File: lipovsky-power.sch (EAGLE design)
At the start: 100 parts, among them Q11 NMOS40V_10A, Q12 NMOS40V_10A, Q14 NMOS40V_10A, Q15 NMOS40V_10A, Q16 NMOS40V_10A, Q18 NMOS40V_10A, Q2 2NMOS30V_0.1A, Q21 PMOS30V_11A, Q22 PMOS30V_11A, Q23 NMOS40V_10A, Q24 NMOS40V_10A, Q25 PMOS30V_11A, Q26 PMOS30V_11A, Q27 NMOS40V_10A, Q28 NMOS40V_10A, Q3 2PMOS50V_0.17A, Q31 PMOS30V_11A, Q32 PMOS30V_11A, Q33 PMOS30V_11A, Q34 PMOS30V_11A, Q35 PMOS30V_11A, Q36 PMOS30V_11A, Q37 PMOS30V_11A, Q38 PMOS30V_11A, Q4 2PMOS50V_0.17A, Q41 PMOS30V_11A, Q42 PMOS30V_11A, Q43 PMOS30V_11A, Q44 PMOS30V_11A, Q45 PMOS30V_11A, Q46 PMOS30V_11A, Q47 PMOS30V_11A, Q48 PMOS30V_11A, Q5 2NMOS30V_0.1A, Q51 PMOS30V_11A, Q52 PMOS30V_11A, Q53 PMOS30V_11A, Q54 PMOS30V_11A, Q55 PMOS30V_11A, Q56 PMOS30V_11A, Q57 PMOS30V_11A, Q58 PMOS30V_11A, Q62 PMOS30V_11A, Q64 PMOS30V_11A, Q66 PMOS30V_11A, Q68 PMOS30V_11A, T1 TFORM_4_4311_4A4, U1 DG508BEN-T1-GE4, U2 DG508BEN-T1-GE4, U3 74HC595, U4 LTC3805-5IDD, U5 TC1240A, U6 AR30N60PPA-13

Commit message: .
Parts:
- removed C6: CAP4.7U_10V, dubec:CAP4.7U_10V
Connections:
- net MVOE renamed GS-2
- net N$7 renamed SENSE
- new net S-SENSE: C2.1, C4.1, D4.A, R5.1, R6.1, U4.GND, U4.OC, U4.SYNC
- net S-: no longer C2.1, C4.1, C6.1, D4.A, R5.1, R6.1, U4.GND, U4.OC, U4.SYNC
- net VCC_REG: no longer C6.2
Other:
- moved on the sheet: C2
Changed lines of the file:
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@@
 <part name="R18" library="dubec" deviceset="RES" device="5.1K_16"/>
 <part name="Q5" library="dubec" deviceset="2NMOS" device="30V_0.1A"/>
-<part name="C6" library="dubec" deviceset="CAP" device="4.7U_10V" value="CAP4.7U_10V"/>
 </parts>
 <sheets>
@@
 <instance part="R7" gate="G$1" x="55.88" y="-66.04"/>
 <instance part="C4" gate="G$1" x="50.8" y="-73.66" rot="R90"/>
-<instance part="C2" gate="G$1" x="53.34" y="-45.72" rot="R90"/>
+<instance part="C2" gate="G$1" x="50.8" y="-45.72" rot="R90"/>
 <instance part="C1" gate="G$1" x="15.24" y="-38.1" rot="R90"/>
 <instance part="C5" gate="G$1" x="73.66" y="-27.94" rot="R90"/>
@@
 <instance part="D2" gate="G$1" x="35.56" y="73.66" rot="R90"/>
 <instance part="D2" gate="G$2" x="27.94" y="53.34" rot="R90"/>
-<instance part="C6" gate="G$1" x="45.72" y="-45.72" rot="R90"/>
 </instances>
 <busses>
@@
 </segment>
 <segment>
-<pinref part="U5" gate="G$1" pin="GND"/>
-<wire x1="30.48" y1="-48.26" x2="30.48" y2="-50.8" width="0.1524" layer="91"/>
-<pinref part="U5" gate="G$1" pin="SHDN"/>
-<pinref part="C2" gate="G$1" pin="1"/>
-<wire x1="76.2" y1="-71.12" x2="76.2" y2="-78.74" width="0.1524" layer="91"/>
-<label x="76.2" y="-81.28" size="1.778" layer="95" rot="R270" xref="yes"/>
-<wire x1="76.2" y1="-78.74" x2="76.2" y2="-81.28" width="0.1524" layer="91"/>
-<junction x="76.2" y="-78.74"/>
-<pinref part="R6" gate="G$1" pin="1"/>
-<wire x1="53.34" y1="-60.96" x2="43.18" y2="-60.96" width="0.1524" layer="91"/>
-<wire x1="43.18" y1="-78.74" x2="50.8" y2="-78.74" width="0.1524" layer="91"/>
-<wire x1="50.8" y1="-78.74" x2="76.2" y2="-78.74" width="0.1524" layer="91"/>
-<wire x1="43.18" y1="-60.96" x2="43.18" y2="-78.74" width="0.1524" layer="91"/>
-<pinref part="C4" gate="G$1" pin="1"/>
-<wire x1="50.8" y1="-76.2" x2="50.8" y2="-78.74" width="0.1524" layer="91"/>
-<junction x="50.8" y="-78.74"/>
-<wire x1="43.18" y1="-50.8" x2="43.18" y2="-60.96" width="0.1524" layer="91"/>
-<junction x="43.18" y="-60.96"/>
-<junction x="43.18" y="-50.8"/>
-<wire x1="30.48" y1="-50.8" x2="40.64" y2="-50.8" width="0.1524" layer="91"/>
-<pinref part="C5" gate="G$1" pin="1"/>
-<wire x1="40.64" y1="-50.8" x2="43.18" y2="-50.8" width="0.1524" layer="91"/>
-<wire x1="73.66" y1="-30.48" x2="73.66" y2="-33.02" width="0.1524" layer="91"/>
-<wire x1="73.66" y1="-33.02" x2="40.64" y2="-33.02" width="0.1524" layer="91"/>
-<pinref part="R5" gate="G$1" pin="1"/>
-<wire x1="104.14" y1="-71.12" x2="104.14" y2="-78.74" width="0.1524" layer="91"/>
-<wire x1="76.2" y1="-78.74" x2="93.98" y2="-78.74" width="0.1524" layer="91"/>
-<wire x1="93.98" y1="-78.74" x2="99.06" y2="-78.74" width="0.1524" layer="91"/>
-<pinref part="U4" gate="G$1" pin="GND"/>
-<pinref part="U4" gate="G$1" pin="SYNC"/>
-<wire x1="99.06" y1="-78.74" x2="104.14" y2="-78.74" width="0.1524" layer="91"/>
-<wire x1="60.96" y1="-50.8" x2="53.34" y2="-50.8" width="0.1524" layer="91"/>
-<pinref part="U4" gate="G$1" pin="OC"/>
-<wire x1="53.34" y1="-50.8" x2="45.72" y2="-50.8" width="0.1524" layer="91"/>
-<wire x1="45.72" y1="-50.8" x2="43.18" y2="-50.8" width="0.1524" layer="91"/>
-<wire x1="91.44" y1="-53.34" x2="93.98" y2="-53.34" width="0.1524" layer="91"/>
-<wire x1="93.98" y1="-53.34" x2="93.98" y2="-78.74" width="0.1524" layer="91"/>
-<junction x="93.98" y="-78.74"/>
-<junction x="104.14" y="-78.74"/>
-<wire x1="119.38" y1="-78.74" x2="104.14" y2="-78.74" width="0.1524" layer="91"/>
-<wire x1="99.06" y1="-71.12" x2="99.06" y2="-78.74" width="0.1524" layer="91"/>
-<junction x="99.06" y="-78.74"/>
-<pinref part="D4" gate="G$1" pin="A"/>
-<pinref part="Q5" gate="G$1" pin="S"/>
-<wire x1="119.38" y1="-60.96" x2="119.38" y2="-78.74" width="0.1524" layer="91"/>
-<pinref part="C6" gate="G$1" pin="1"/>
-<junction x="45.72" y="-50.8"/>
-<wire x1="40.64" y1="-33.02" x2="40.64" y2="-50.8" width="0.1524" layer="91"/>
-<junction x="40.64" y="-33.02"/>
-<junction x="40.64" y="-50.8"/>
-<wire x1="53.34" y1="-48.26" x2="53.34" y2="-50.8" width="0.1524" layer="91"/>
-<junction x="53.34" y="-50.8"/>
-<wire x1="45.72" y1="-48.26" x2="45.72" y2="-50.8" width="0.1524" layer="91"/>
-</segment>
-<segment>
 <pinref part="U1" gate="G$1" pin="GND"/>
 <wire x1="121.92" y1="76.2" x2="124.46" y2="76.2" width="0.1524" layer="91"/>
@@
 <pinref part="C8" gate="G$1" pin="1"/>
 <wire x1="241.3" y1="76.2" x2="259.08" y2="76.2" width="0.1524" layer="91"/>
+</segment>
+<segment>
+<pinref part="U5" gate="G$1" pin="GND"/>
+<wire x1="30.48" y1="-48.26" x2="30.48" y2="-50.8" width="0.1524" layer="91"/>
+<wire x1="30.48" y1="-50.8" x2="40.64" y2="-50.8" width="0.1524" layer="91"/>
+<pinref part="U5" gate="G$1" pin="SHDN"/>
+<pinref part="C5" gate="G$1" pin="1"/>
+<wire x1="73.66" y1="-30.48" x2="73.66" y2="-33.02" width="0.1524" layer="91"/>
+<wire x1="73.66" y1="-33.02" x2="40.64" y2="-33.02" width="0.1524" layer="91"/>
+<wire x1="40.64" y1="-33.02" x2="40.64" y2="-50.8" width="0.1524" layer="91"/>
+<junction x="40.64" y="-33.02"/>
+<label x="30.48" y="-53.34" size="1.778" layer="95" rot="R270" xref="yes"/>
+<wire x1="30.48" y1="-50.8" x2="30.48" y2="-53.34" width="0.1524" layer="91"/>
+<junction x="30.48" y="-50.8"/>
+</segment>
+<segment>
+<pinref part="Q5" gate="G$1" pin="S"/>
+<wire x1="119.38" y1="-60.96" x2="119.38" y2="-68.58" width="0.1524" layer="91"/>
+<label x="119.38" y="-68.58" size="1.778" layer="95" rot="R270" xref="yes"/>
 </segment>
 </net>
@@
 </segment>
 </net>
-<net name="MVOE" class="0">
+<net name="GS-2" class="0">
 <segment>
 <pinref part="Q23" gate="G$1" pin="G"/>
@@
 <pinref part="U5" gate="G$1" pin="VOUT"/>
 <wire x1="40.64" y1="-38.1" x2="43.18" y2="-38.1" width="0.1524" layer="91"/>
-<wire x1="43.18" y1="-38.1" x2="45.72" y2="-38.1" width="0.1524" layer="91"/>
-<wire x1="45.72" y1="-38.1" x2="53.34" y2="-38.1" width="0.1524" layer="91"/>
-<wire x1="53.34" y1="-38.1" x2="76.2" y2="-38.1" width="0.1524" layer="91"/>
+<wire x1="43.18" y1="-38.1" x2="50.8" y2="-38.1" width="0.1524" layer="91"/>
+<wire x1="50.8" y1="-38.1" x2="76.2" y2="-38.1" width="0.1524" layer="91"/>
 <wire x1="76.2" y1="-38.1" x2="76.2" y2="-40.64" width="0.1524" layer="91"/>
 <junction x="43.18" y="-38.1"/>
@@
 <wire x1="76.2" y1="-38.1" x2="119.38" y2="-38.1" width="0.1524" layer="91"/>
 <wire x1="119.38" y1="-38.1" x2="119.38" y2="-40.64" width="0.1524" layer="91"/>
-<junction x="45.72" y="-38.1"/>
-<pinref part="C6" gate="G$1" pin="2"/>
-<wire x1="45.72" y1="-40.64" x2="45.72" y2="-38.1" width="0.1524" layer="91"/>
-<wire x1="53.34" y1="-38.1" x2="53.34" y2="-40.64" width="0.1524" layer="91"/>
-<junction x="53.34" y="-38.1"/>
+<wire x1="50.8" y1="-38.1" x2="50.8" y2="-40.64" width="0.1524" layer="91"/>
+<junction x="50.8" y="-38.1"/>
 </segment>
 </net>
@@
 </segment>
 </net>
-<net name="N$7" class="0">
+<net name="SENSE" class="0">
 <segment>
 <pinref part="MVOE" gate="G$1" pin="S"/>
@@
 </segment>
 </net>
+<net name="S-SENSE" class="0">
+<segment>
+<pinref part="C2" gate="G$1" pin="1"/>
+<label x="43.18" y="-78.74" size="1.778" layer="95" rot="R180" xref="yes"/>
+<pinref part="R6" gate="G$1" pin="1"/>
+<wire x1="53.34" y1="-60.96" x2="45.72" y2="-60.96" width="0.1524" layer="91"/>
+<wire x1="45.72" y1="-78.74" x2="50.8" y2="-78.74" width="0.1524" layer="91"/>
+<wire x1="50.8" y1="-78.74" x2="76.2" y2="-78.74" width="0.1524" layer="91"/>
+<wire x1="45.72" y1="-60.96" x2="45.72" y2="-78.74" width="0.1524" layer="91"/>
+<pinref part="C4" gate="G$1" pin="1"/>
+<wire x1="50.8" y1="-76.2" x2="50.8" y2="-78.74" width="0.1524" layer="91"/>
+<junction x="50.8" y="-78.74"/>
+<wire x1="45.72" y1="-50.8" x2="45.72" y2="-60.96" width="0.1524" layer="91"/>
+<junction x="45.72" y="-60.96"/>
+<pinref part="U4" gate="G$1" pin="SYNC"/>
+<wire x1="60.96" y1="-50.8" x2="50.8" y2="-50.8" width="0.1524" layer="91"/>
+<wire x1="50.8" y1="-50.8" x2="45.72" y2="-50.8" width="0.1524" layer="91"/>
+<wire x1="50.8" y1="-48.26" x2="50.8" y2="-50.8" width="0.1524" layer="91"/>
+<junction x="50.8" y="-50.8"/>
+<pinref part="R5" gate="G$1" pin="1"/>
+<wire x1="104.14" y1="-71.12" x2="104.14" y2="-78.74" width="0.1524" layer="91"/>
+<wire x1="99.06" y1="-78.74" x2="104.14" y2="-78.74" width="0.1524" layer="91"/>
+<pinref part="D4" gate="G$1" pin="A"/>
+<wire x1="99.06" y1="-71.12" x2="99.06" y2="-78.74" width="0.1524" layer="91"/>
+<junction x="99.06" y="-78.74"/>
+<wire x1="93.98" y1="-78.74" x2="99.06" y2="-78.74" width="0.1524" layer="91"/>
+<pinref part="U4" gate="G$1" pin="OC"/>
+<wire x1="91.44" y1="-53.34" x2="93.98" y2="-53.34" width="0.1524" layer="91"/>
+<wire x1="93.98" y1="-53.34" x2="93.98" y2="-78.74" width="0.1524" layer="91"/>
+<wire x1="76.2" y1="-78.74" x2="93.98" y2="-78.74" width="0.1524" layer="91"/>
+<junction x="76.2" y="-78.74"/>
+<junction x="93.98" y="-78.74"/>
+<pinref part="U4" gate="G$1" pin="GND"/>
+<wire x1="76.2" y1="-78.74" x2="76.2" y2="-71.12" width="0.1524" layer="91"/>
+<wire x1="45.72" y1="-78.74" x2="43.18" y2="-78.74" width="0.1524" layer="91"/>
+<junction x="45.72" y="-78.74"/>
+</segment>
+</net>

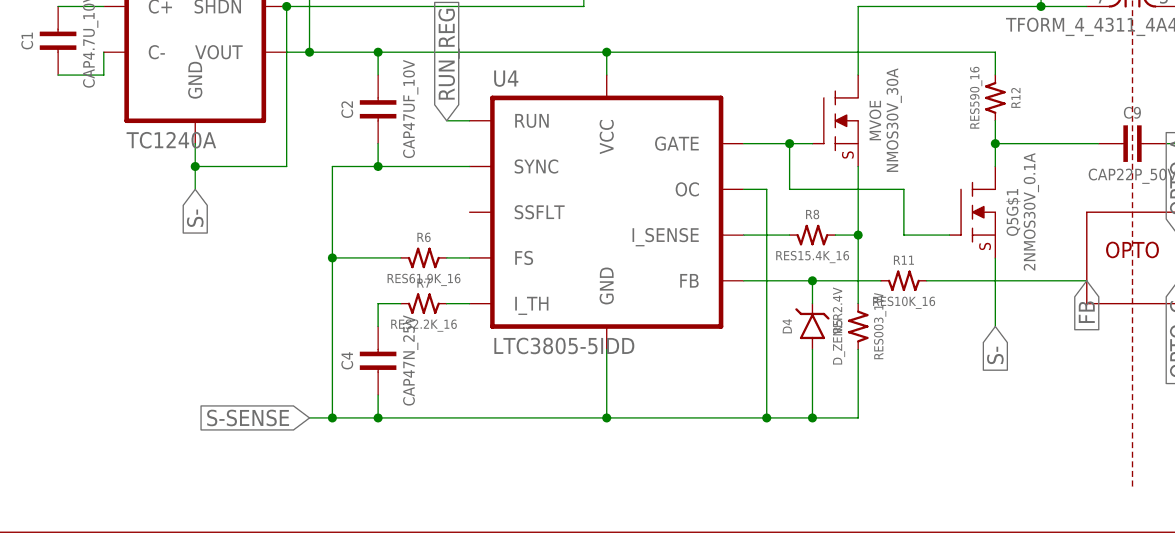
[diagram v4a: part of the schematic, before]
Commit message: Removed separate S-_SENSE
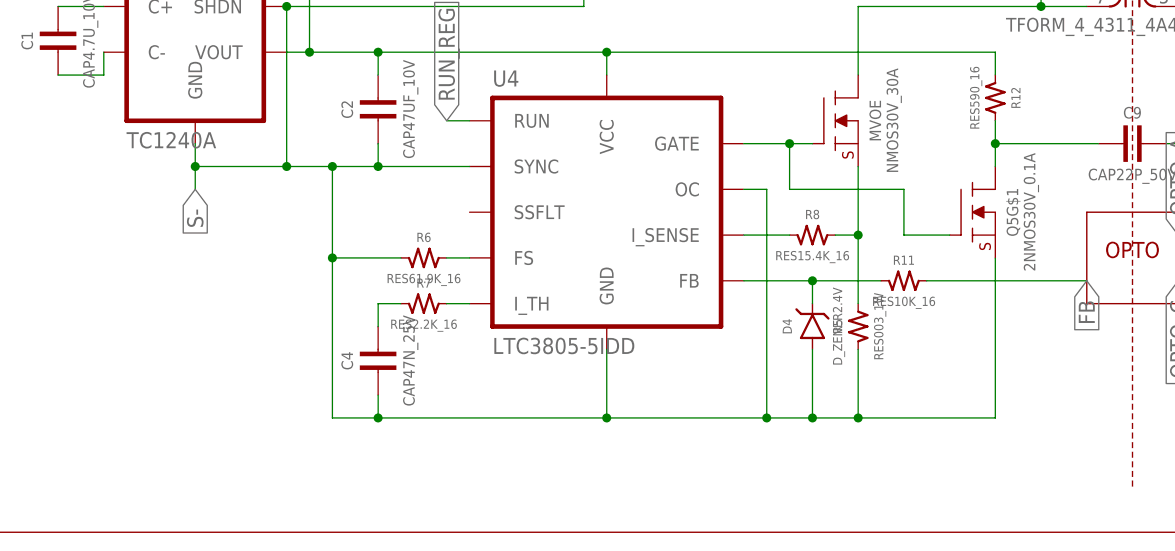
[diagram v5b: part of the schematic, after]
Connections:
- removed net S-SENSE: C2.1, C4.1, D4.A, R5.1, R6.1, U4.GND, U4.OC, U4.SYNC
- net S-: now also C2.1, C4.1, D4.A, R5.1, R6.1, U4.GND, U4.OC, U4.SYNC
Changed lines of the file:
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@@
 <wire x1="30.48" y1="-50.8" x2="30.48" y2="-53.34" width="0.1524" layer="91"/>
 <junction x="30.48" y="-50.8"/>
-</segment>
-<segment>
+<pinref part="C2" gate="G$1" pin="1"/>
+<pinref part="R6" gate="G$1" pin="1"/>
+<wire x1="53.34" y1="-60.96" x2="45.72" y2="-60.96" width="0.1524" layer="91"/>
+<wire x1="45.72" y1="-78.74" x2="50.8" y2="-78.74" width="0.1524" layer="91"/>
+<wire x1="50.8" y1="-78.74" x2="76.2" y2="-78.74" width="0.1524" layer="91"/>
+<wire x1="45.72" y1="-60.96" x2="45.72" y2="-78.74" width="0.1524" layer="91"/>
+<pinref part="C4" gate="G$1" pin="1"/>
+<wire x1="50.8" y1="-76.2" x2="50.8" y2="-78.74" width="0.1524" layer="91"/>
+<junction x="50.8" y="-78.74"/>
+<wire x1="45.72" y1="-50.8" x2="45.72" y2="-60.96" width="0.1524" layer="91"/>
+<junction x="45.72" y="-60.96"/>
+<pinref part="U4" gate="G$1" pin="SYNC"/>
+<wire x1="60.96" y1="-50.8" x2="50.8" y2="-50.8" width="0.1524" layer="91"/>
+<wire x1="50.8" y1="-50.8" x2="45.72" y2="-50.8" width="0.1524" layer="91"/>
+<wire x1="50.8" y1="-48.26" x2="50.8" y2="-50.8" width="0.1524" layer="91"/>
+<junction x="50.8" y="-50.8"/>
+<pinref part="R5" gate="G$1" pin="1"/>
+<wire x1="104.14" y1="-71.12" x2="104.14" y2="-78.74" width="0.1524" layer="91"/>
+<wire x1="99.06" y1="-78.74" x2="104.14" y2="-78.74" width="0.1524" layer="91"/>
+<pinref part="D4" gate="G$1" pin="A"/>
+<wire x1="99.06" y1="-71.12" x2="99.06" y2="-78.74" width="0.1524" layer="91"/>
+<junction x="99.06" y="-78.74"/>
+<wire x1="93.98" y1="-78.74" x2="99.06" y2="-78.74" width="0.1524" layer="91"/>
+<pinref part="U4" gate="G$1" pin="OC"/>
+<wire x1="91.44" y1="-53.34" x2="93.98" y2="-53.34" width="0.1524" layer="91"/>
+<wire x1="93.98" y1="-53.34" x2="93.98" y2="-78.74" width="0.1524" layer="91"/>
+<wire x1="76.2" y1="-78.74" x2="93.98" y2="-78.74" width="0.1524" layer="91"/>
+<junction x="76.2" y="-78.74"/>
+<junction x="93.98" y="-78.74"/>
+<pinref part="U4" gate="G$1" pin="GND"/>
+<wire x1="76.2" y1="-78.74" x2="76.2" y2="-71.12" width="0.1524" layer="91"/>
+<wire x1="40.64" y1="-50.8" x2="45.72" y2="-50.8" width="0.1524" layer="91"/>
+<junction x="40.64" y="-50.8"/>
+<junction x="45.72" y="-50.8"/>
+<wire x1="104.14" y1="-78.74" x2="119.38" y2="-78.74" width="0.1524" layer="91"/>
+<junction x="104.14" y="-78.74"/>
 <pinref part="Q5" gate="G$1" pin="S"/>
-<wire x1="119.38" y1="-60.96" x2="119.38" y2="-68.58" width="0.1524" layer="91"/>
-<label x="119.38" y="-68.58" size="1.778" layer="95" rot="R270" xref="yes"/>
+<wire x1="119.38" y1="-78.74" x2="119.38" y2="-60.96" width="0.1524" layer="91"/>
 </segment>
 </net>
@@
 </segment>
 </net>
-<net name="S-SENSE" class="0">
-<segment>
-<pinref part="C2" gate="G$1" pin="1"/>
-<label x="43.18" y="-78.74" size="1.778" layer="95" rot="R180" xref="yes"/>
-<pinref part="R6" gate="G$1" pin="1"/>
-<wire x1="53.34" y1="-60.96" x2="45.72" y2="-60.96" width="0.1524" layer="91"/>
-<wire x1="45.72" y1="-78.74" x2="50.8" y2="-78.74" width="0.1524" layer="91"/>
-<wire x1="50.8" y1="-78.74" x2="76.2" y2="-78.74" width="0.1524" layer="91"/>
-<wire x1="45.72" y1="-60.96" x2="45.72" y2="-78.74" width="0.1524" layer="91"/>
-<pinref part="C4" gate="G$1" pin="1"/>
-<wire x1="50.8" y1="-76.2" x2="50.8" y2="-78.74" width="0.1524" layer="91"/>
-<junction x="50.8" y="-78.74"/>
-<wire x1="45.72" y1="-50.8" x2="45.72" y2="-60.96" width="0.1524" layer="91"/>
-<junction x="45.72" y="-60.96"/>
-<pinref part="U4" gate="G$1" pin="SYNC"/>
-<wire x1="60.96" y1="-50.8" x2="50.8" y2="-50.8" width="0.1524" layer="91"/>
-<wire x1="50.8" y1="-50.8" x2="45.72" y2="-50.8" width="0.1524" layer="91"/>
-<wire x1="50.8" y1="-48.26" x2="50.8" y2="-50.8" width="0.1524" layer="91"/>
-<junction x="50.8" y="-50.8"/>
-<pinref part="R5" gate="G$1" pin="1"/>
-<wire x1="104.14" y1="-71.12" x2="104.14" y2="-78.74" width="0.1524" layer="91"/>
-<wire x1="99.06" y1="-78.74" x2="104.14" y2="-78.74" width="0.1524" layer="91"/>
-<pinref part="D4" gate="G$1" pin="A"/>
-<wire x1="99.06" y1="-71.12" x2="99.06" y2="-78.74" width="0.1524" layer="91"/>
-<junction x="99.06" y="-78.74"/>
-<wire x1="93.98" y1="-78.74" x2="99.06" y2="-78.74" width="0.1524" layer="91"/>
-<pinref part="U4" gate="G$1" pin="OC"/>
-<wire x1="91.44" y1="-53.34" x2="93.98" y2="-53.34" width="0.1524" layer="91"/>
-<wire x1="93.98" y1="-53.34" x2="93.98" y2="-78.74" width="0.1524" layer="91"/>
-<wire x1="76.2" y1="-78.74" x2="93.98" y2="-78.74" width="0.1524" layer="91"/>
-<junction x="76.2" y="-78.74"/>
-<junction x="93.98" y="-78.74"/>
-<pinref part="U4" gate="G$1" pin="GND"/>
-<wire x1="76.2" y1="-78.74" x2="76.2" y2="-71.12" width="0.1524" layer="91"/>
-<wire x1="45.72" y1="-78.74" x2="43.18" y2="-78.74" width="0.1524" layer="91"/>
-<junction x="45.72" y="-78.74"/>
-</segment>
-</net>
